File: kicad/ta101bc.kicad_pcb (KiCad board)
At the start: 2 copper layers, 83.8 x 64.8 mm, 99 parts, among them J1 INPUT, J2 OUTPUT, J3 SUBSONIC, J4 POWER, J5 MM INPUT, J6 PHONO, J7 OUTPUT, J8 SUPPLY+, Q1 BC549C, Q101 BC549C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

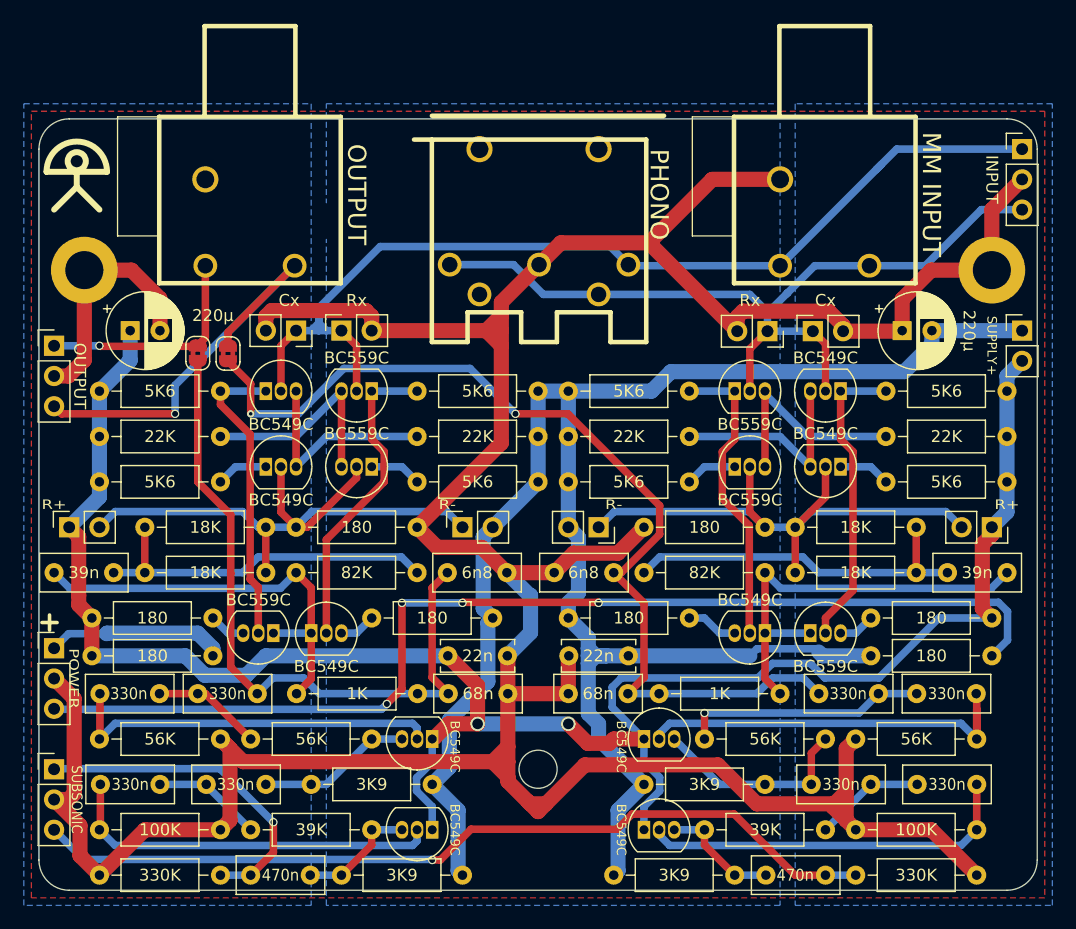
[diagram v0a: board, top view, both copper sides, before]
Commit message: fix form factor
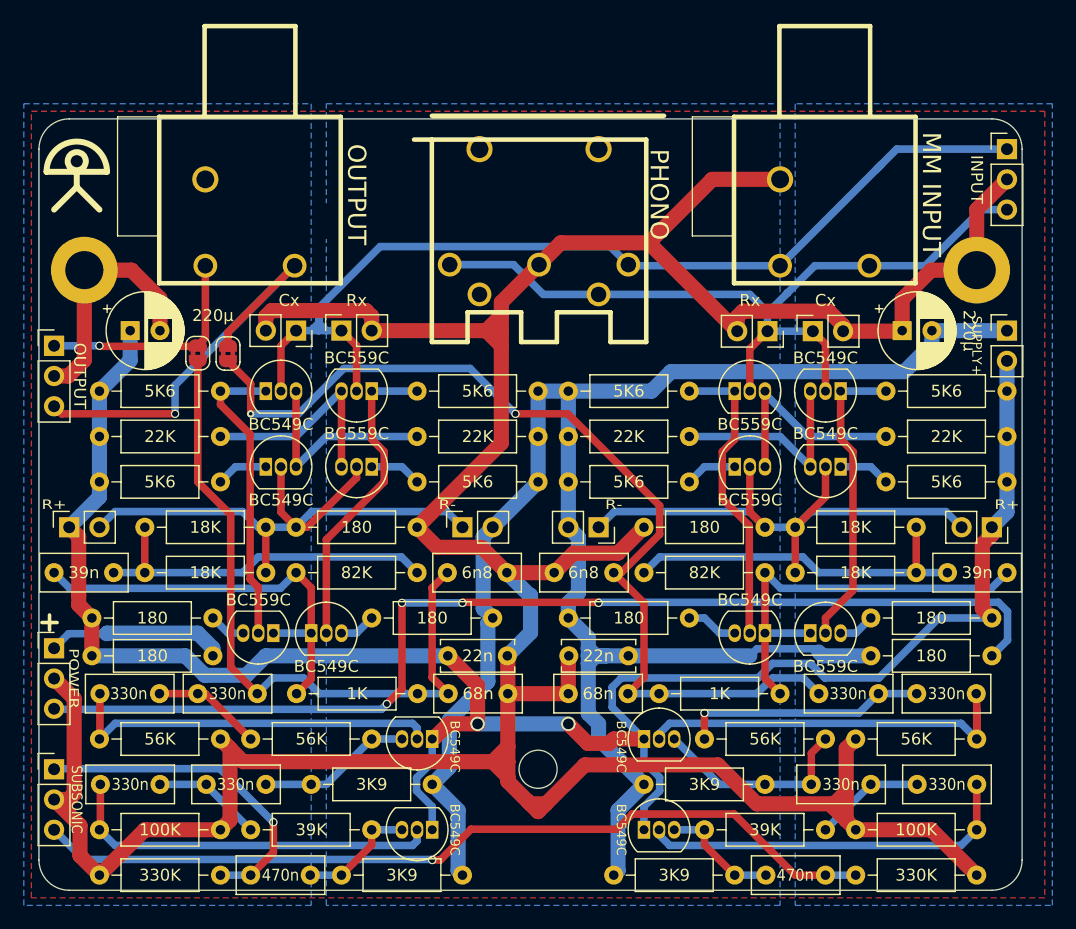
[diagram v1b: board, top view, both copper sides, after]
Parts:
- moved H2 1.27 mm to (104.1, 38.1)
- moved J1 1.27 mm to (106.7, 27.9)
- moved J8 1.27 mm to (106.7, 43.2)
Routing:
- net GND: track 319.2 -> 317.9 mm
- net /IN': track 70.0 -> 68.8 mm
- net /IN: track 85.9 -> 84.6 mm
- net /F-9: track 161.3 -> 160.1 mm
- net /F+9: track 168.6 -> 168.1 mm
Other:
- board size 83.8 x 64.8 mm -> 82.6 x 64.8 mm
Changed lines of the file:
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@@
 	(footprint "MountingHole:MountingHole_3.2mm_M3_DIN965_Pad"
 		(layer "F.Cu")
-		(at 105.41 38.1)
+		(at 104.14 38.1)
 		(descr "Mounting Hole 3.2mm, M3, DIN965")
 		(tags "mounting hole 3.2mm m3 din965")
@@
 	(footprint "Connector_PinHeader_2.54mm:PinHeader_1x02_P2.54mm_Vertical"
 		(layer "F.Cu")
-		(at 107.95 43.18)
+		(at 106.68 43.18)
 		(descr "Through hole straight pin header, 1x02, 2.54mm pitch, single row")
 		(tags "Through hole pin header THT 1x02 2.54mm single row")
@@
 		)
 		(property "Value" "SUBSONIC"
-			(at 1.905 2.54 270)
+			(at 1.905 2.54 -90)
 			(unlocked yes)
 			(layer "F.SilkS")
@@
 	(footprint "Connector_PinHeader_2.54mm:PinHeader_1x03_P2.54mm_Vertical"
 		(layer "F.Cu")
-		(at 107.95 27.94)
+		(at 106.68 27.94)
 		(descr "Through hole straight pin header, 1x03, 2.54mm pitch, single row")
 		(tags "Through hole pin header THT 1x03 2.54mm single row")
@@
 	)
 	(gr_arc
-		(start 106.68 25.4)
-		(mid 108.476051 26.143949)
-		(end 109.22 27.94)
+		(start 105.41 25.4)
+		(mid 107.206051 26.143949)
+		(end 107.95 27.94)
 		(stroke
 			(width 0.05)
@@
 	)
 	(gr_arc
-		(start 109.22 87.63)
-		(mid 108.476051 89.426051)
-		(end 106.68 90.17)
+		(start 107.95 87.63)
+		(mid 107.206051 89.426051)
+		(end 105.41 90.17)
 		(stroke
 			(width 0.05)
@@
 	(gr_line
 		(start 27.94 90.17)
-		(end 106.68 90.17)
+		(end 105.41 90.17)
 		(stroke
 			(width 0.05)
@@
 	)
 	(gr_line
-		(start 109.22 27.94)
-		(end 109.22 87.63)
+		(start 107.95 27.94)
+		(end 107.95 87.63)
 		(stroke
 			(width 0.05)
@@
 	(gr_line
 		(start 27.94 25.4)
-		(end 106.68 25.4)
+		(end 105.41 25.4)
 		(stroke
 			(width 0.05)
@@
 	)
 	(segment
-		(start 100.33 38.1)
-		(end 105.41 38.1)
-		(width 1.27)
-		(layer "F.Cu")
-		(net 3)
-	)
-	(segment
 		(start 66.484126 82.740874)
 		(end 66.658252 82.915)
@@
 	)
 	(segment
-		(start 105.41 38.1)
-		(end 105.41 33.02)
+		(start 104.14 33.02)
+		(end 106.68 30.48)
 		(width 1.27)
 		(layer "F.Cu")
@@
 	)
 	(segment
+		(start 100.33 38.1)
+		(end 104.14 38.1)
+		(width 1.27)
+		(layer "F.Cu")
+		(net 3)
+	)
+	(segment
 		(start 58.835 61.375)
 		(end 57.15 59.69)
@@
 	)
 	(segment
+		(start 104.14 38.1)
+		(end 104.14 33.02)
+		(width 1.27)
+		(layer "F.Cu")
+		(net 3)
+	)
+	(segment
 		(start 69.225 35.805)
 		(end 76.605 35.805)
@@
 	)
 	(segment
-		(start 105.41 33.02)
-		(end 107.95 30.48)
-		(width 1.27)
-		(layer "F.Cu")
-		(net 3)
-	)
-	(segment
 		(start 64.77 70.525)
 		(end 64.73 70.485)
@@
 	)
 	(segment
-		(start 95.9325 72.3425)
-		(end 100.965 67.31)
-		(width 0.635)
+		(start 106.68 48.26)
+		(end 106.68 45.72)
+		(width 1.27)
 		(layer "B.Cu")
 		(net 12)
 	)
 	(segment
-		(start 106.68 46.99)
-		(end 107.95 45.72)
-		(width 1.27)
+		(start 95.9325 72.3425)
+		(end 100.965 67.31)
+		(width 0.635)
 		(layer "B.Cu")
 		(net 12)
@@
 	)
 	(segment
-		(start 106.68 48.26)
-		(end 106.68 46.99)
-		(width 1.27)
-		(layer "B.Cu")
-		(net 12)
-	)
-	(segment
 		(start 77.5175 81.825727)
 		(end 77.5175 80.6925)
@@
 	)
 	(segment
+		(start 106.68 43.18)
+		(end 100.377621 43.18)
+		(width 1.27)
+		(layer "B.Cu")
+		(net 13)
+	)
+	(segment
 		(start 98.063991 46.625)
 		(end 100.377621 44.31137)
@@
 	)
 	(segment
-		(start 100.377621 43.18)
-		(end 107.95 43.18)
-		(width 1.27)
-		(layer "B.Cu")
-		(net 13)
-	)
-	(segment
 		(start 71.525 70.485)
 		(end 73.025 70.485)
@@
 	)
 	(segment
-		(start 107.95 27.94)
-		(end 97.42 27.94)
-		(width 0.635)
-		(layer "B.Cu")
-		(net 14)
-	)
-	(segment
 		(start 48.895 41.91)
 		(end 48.895 43.18)
@@
 	)
 	(segment
+		(start 97.42 27.94)
+		(end 106.68 27.94)
+		(width 0.635)
+		(layer "B.Cu")
+		(net 14)
+	)
+	(segment
 		(start 48.895 41.91)
 		(end 48.895 42.545)
@@
 	)
 	(segment
-		(start 95.13 37.73)
-		(end 99.818346 37.73)
+		(start 104.528346 33.02)
+		(end 106.68 33.02)
 		(width 0.635)
 		(layer "B.Cu")
@@
 	)
 	(segment
-		(start 59.89 37.64)
-		(end 65.24393 37.64)
+		(start 95.13 37.73)
+		(end 99.818346 37.73)
 		(width 0.635)
 		(layer "B.Cu")
@@
 	)
 	(segment
-		(start 104.528346 33.02)
-		(end 107.95 33.02)
+		(start 59.89 37.64)
+		(end 65.24393 37.64)
 		(width 0.635)
 		(layer "B.Cu")

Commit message: MC resistor option, improve silkscreen
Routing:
- net /SUBS': track 72.1 -> 73.9 mm
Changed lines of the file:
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@@
 		)
 		(property "Value" "220µ"
-			(at 5.627379 0 -90)
+			(at -1.377621 3.32 0)
 			(unlocked yes)
 			(layer "F.SilkS")
@@
 					(size 1 1)
 					(thickness 0.15)
+					(italic yes)
 				)
 			)
@@
 					(size 1 1)
 					(thickness 0.15)
+					(italic yes)
 				)
 			)
@@
 		)
 		(property "Value" "SUPPLY+"
-			(at -2.54 1.27 -90)
+			(at -2.54 0.82 270)
 			(unlocked yes)
 			(layer "F.SilkS")
 			(effects
 				(font
-					(size 0.8 0.8)
+					(size 0.8 0.75)
 					(thickness 0.15)
 				)
@@
 	)
 	(segment
-		(start 83.7725 83.7725)
-		(end 88.9 88.9)
+		(start 88.9 88.9)
+		(end 91.44 88.9)
 		(width 0.635)
 		(layer "F.Cu")
@@
 	)
 	(segment
-		(start 88.9 88.9)
-		(end 91.44 88.9)
+		(start 61.286614 87.363387)
+		(end 63.423227 89.5)
 		(width 0.635)
 		(layer "F.Cu")
@@
 	)
 	(segment
-		(start 61.684274 85.0425)
-		(end 73.9375 85.0425)
+		(start 60.233387 87.63)
+		(end 60.5 87.363387)
 		(width 0.635)
 		(layer "F.Cu")
@@
 	)
 	(segment
-		(start 73.9375 85.0425)
+		(start 69.48 89.5)
 		(end 75.2075 83.7725)
 		(width 0.635)
@@
 	)
 	(segment
-		(start 59.096773 87.63)
-		(end 60.980887 85.745887)
+		(start 60.5 87.363387)
+		(end 61.286614 87.363387)
+		(width 0.635)
+		(layer "F.Cu")
+		(net 24)
+	)
+	(segment
+		(start 83.7725 83.7725)
+		(end 88.9 88.9)
 		(width 0.635)
 		(layer "F.Cu")
@@
 	)
 	(segment
-		(start 60.980887 85.745887)
-		(end 61.684274 85.0425)
+		(start 63.423227 89.5)
+		(end 69.48 89.5)
 		(width 0.635)
 		(layer "F.Cu")
@@
 	(segment
 		(start 58.42 87.63)
-		(end 59.096773 87.63)
+		(end 60.233387 87.63)
 		(width 0.635)
 		(layer "F.Cu")
